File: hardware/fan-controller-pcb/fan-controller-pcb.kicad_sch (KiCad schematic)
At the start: 42 parts, among them J1 Screw_Terminal_01x04, J2 nc3fdm3-v, J3 nc3mdm3-v, SW2 SW_DIP_x10, U2 MC7805CDTG, U3 MCP4922, U4 TLC272, U5 MAX485E

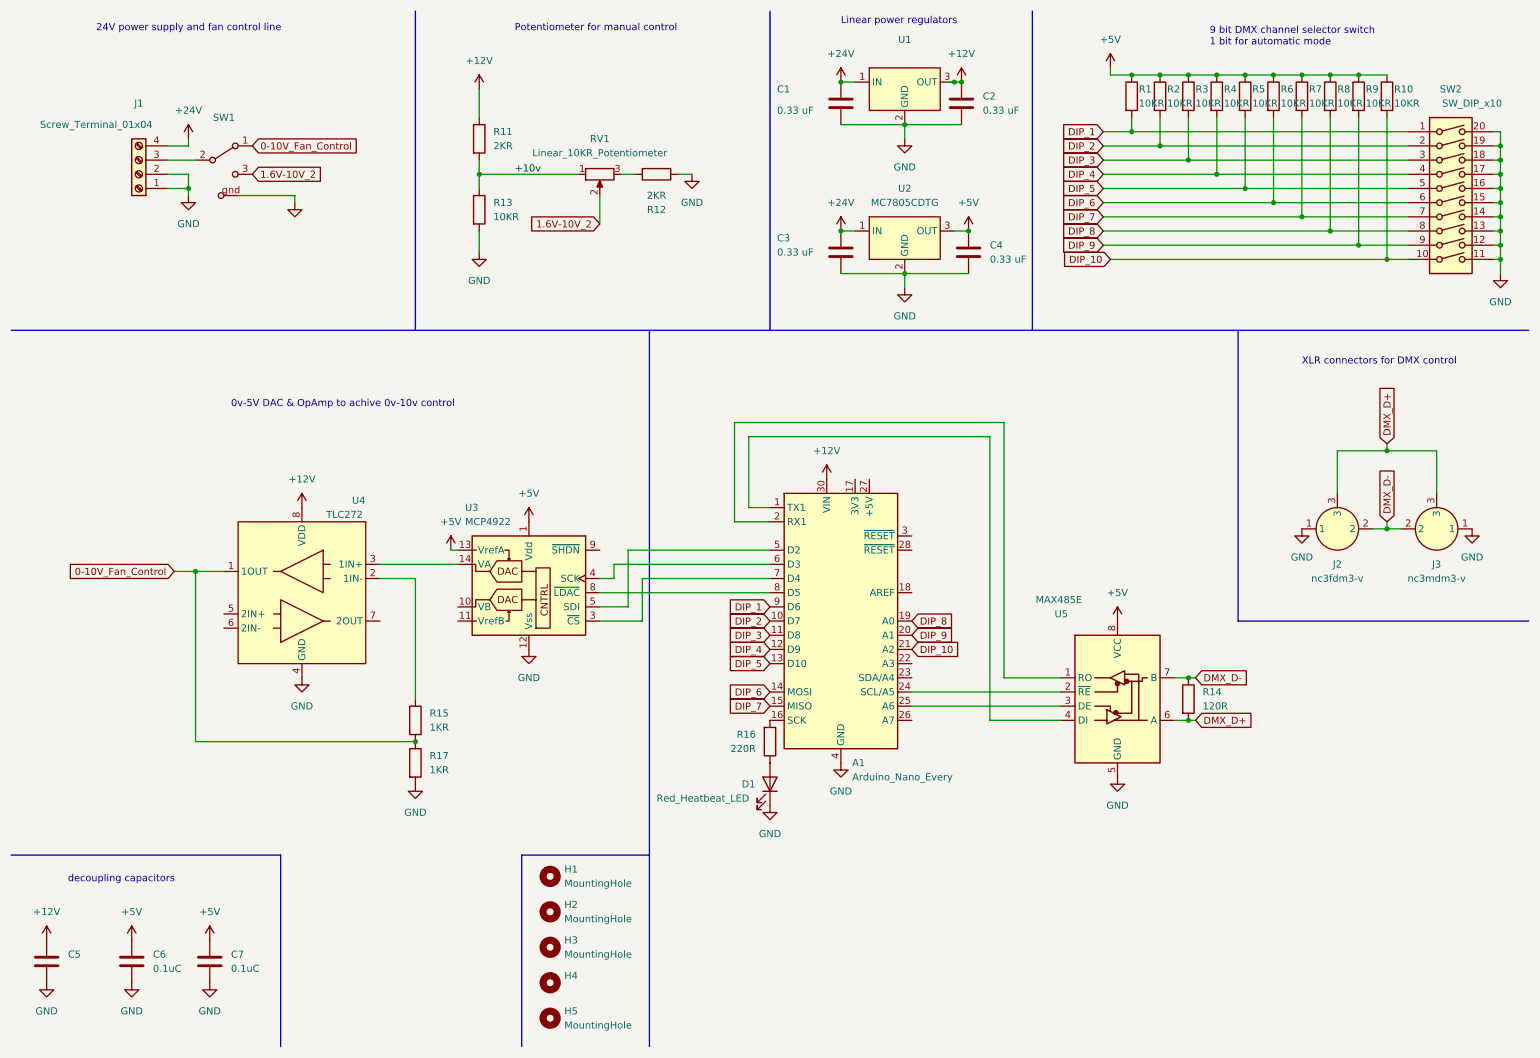
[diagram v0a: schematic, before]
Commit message: update PCB: edge cuts, routing, symbol_lib, footprint_lib, art & data sheets
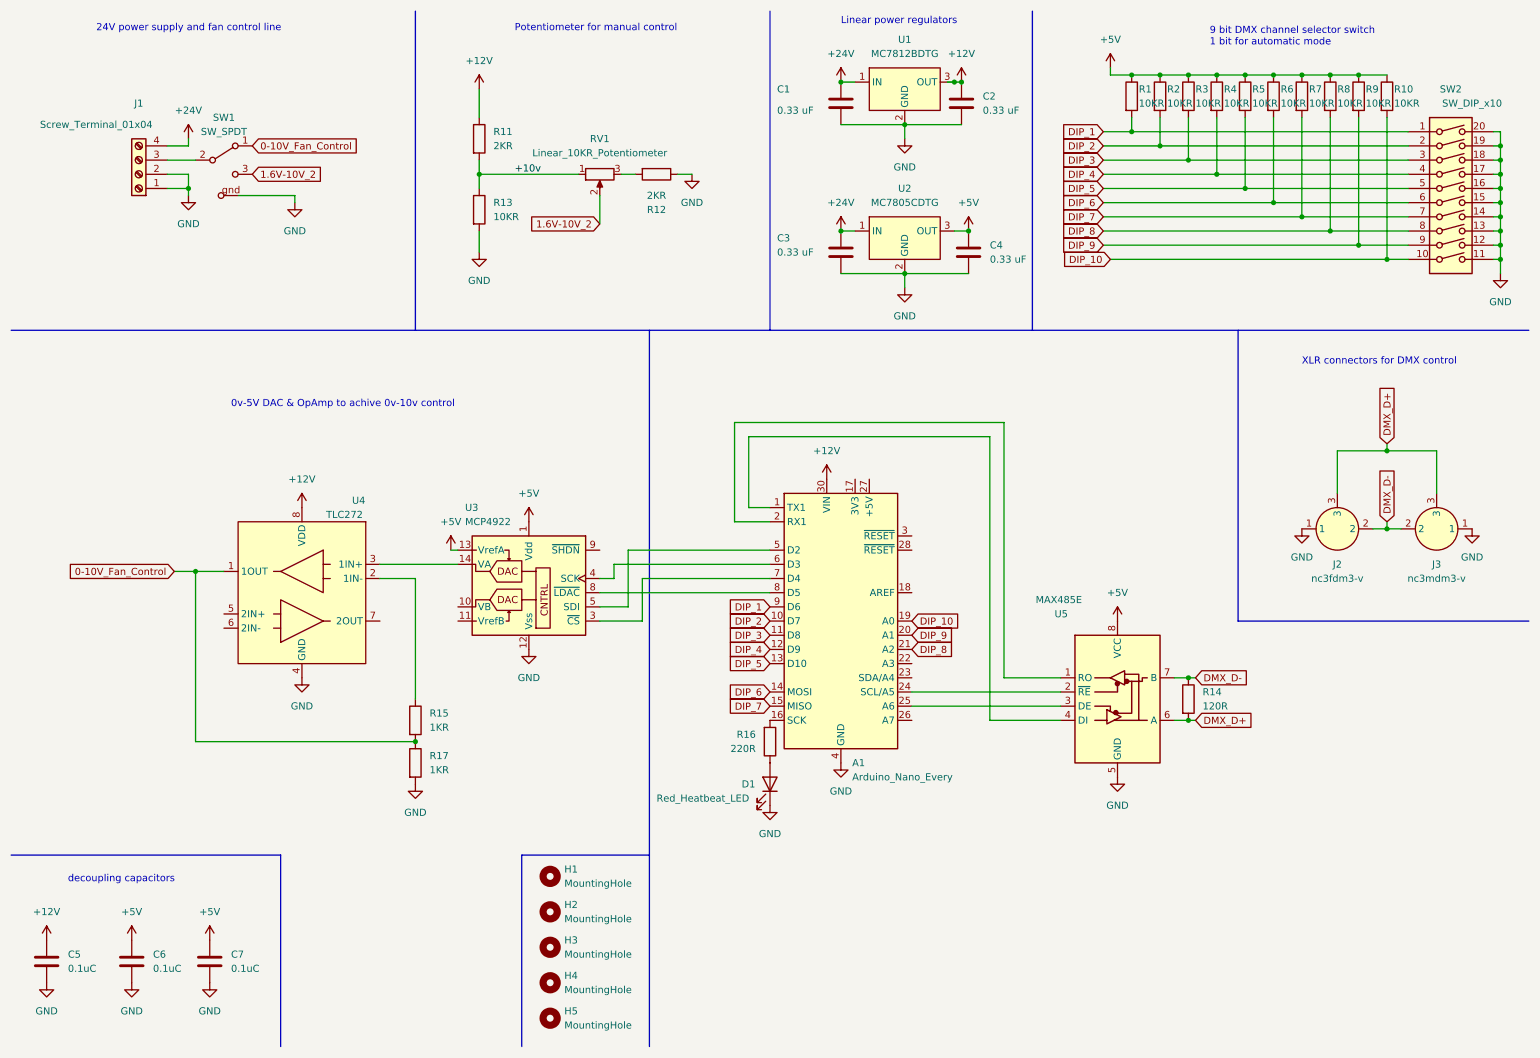
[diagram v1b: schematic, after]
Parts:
- A1: footprint (none) -> Module:Arduino_Nano
- C5: value (none) -> 0.1uC; footprint (none) -> Capacitor_SMD:C_0805_2012Metric
- C6, C7: footprint (none) -> Capacitor_SMD:C_0805_2012Metric
- H1, H2, H3, H5: footprint (none) -> MountingHole:MountingHole_3.2mm_M3_ISO14580_Pad_TopBottom
- H4: value (none) -> MountingHole; footprint (none) -> MountingHole:MountingHole_3.2mm_M3_ISO14580_Pad_TopBottom
- SW1: value (none) -> SW_SPDT; footprint (none) -> Switch:WS-TOTV_6.35_Right_Angle_Toggle_Switch
- U1: value (none) -> MC7812BDTG; footprint (none) -> Voltage_Regulator:MC7812BDTG
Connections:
- net DIP_10: now also A1.19 (A0); no longer A1.21 (A2)
- net DIP_8: now also A1.21 (A2); no longer A1.19 (A0)
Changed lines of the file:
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@@
     )
   )
-  (global_label "DIP_8" (shape input) (at 173.99 121.92 0) (fields_autoplaced)
+  (global_label "DIP_8" (shape input) (at 173.99 127 0) (fields_autoplaced)
     (effects (font (size 1.27 1.27)) (justify left))
-    (property "Intersheet References" "${INTERSHEET_REFS}" (id 0) (at 181.725 121.8406 0)
+    (property "Intersheet References" "${INTERSHEET_REFS}" (id 0) (at 181.725 126.9206 0)
       (effects (font (size 1.27 1.27)) (justify left) hide)
     )
@@
     )
   )
-  (global_label "DIP_10" (shape input) (at 173.99 127 0) (fields_autoplaced)
+  (global_label "DIP_10" (shape input) (at 173.99 121.92 0) (fields_autoplaced)
     (effects (font (size 1.27 1.27)) (justify left))
-    (property "Intersheet References" "${INTERSHEET_REFS}" (id 0) (at 182.9345 126.9206 0)
+    (property "Intersheet References" "${INTERSHEET_REFS}" (id 0) (at 182.9345 121.8406 0)
       (effects (font (size 1.27 1.27)) (justify left) hide)
     )
@@
     (in_bom yes) (on_board yes) (fields_autoplaced)
     (property "Reference" "SW1" (id 0) (at 50.8 31.75 0))
-    (property "Value" "" (id 1) (at 50.8 34.29 0))
-    (property "Footprint" "" (id 2) (at 50.8 39.37 0)
+    (property "Value" "SW_SPDT" (id 1) (at 50.8 34.29 0))
+    (property "Footprint" "Switch:WS-TOTV_6.35_Right_Angle_Toggle_Switch" (id 2) (at 50.8 39.37 0)
       (effects (font (size 1.27 1.27)) hide)
     )
@@
       (effects (font (size 1.27 1.27)) (justify left))
     )
-    (property "Footprint" "" (id 2) (at 49.2252 186.69 0)
+    (property "Footprint" "Capacitor_SMD:C_0805_2012Metric" (id 2) (at 49.2252 186.69 0)
       (effects (font (size 1.27 1.27)) hide)
     )
@@
       (effects (font (size 1.27 1.27)) (justify left))
     )
-    (property "Value" "" (id 1) (at 111.76 187.9599 0)
-      (effects (font (size 1.27 1.27)) (justify left))
-    )
-    (property "Footprint" "" (id 2) (at 109.22 186.69 0)
+    (property "Value" "MountingHole" (id 1) (at 111.76 187.9599 0)
+      (effects (font (size 1.27 1.27)) (justify left))
+    )
+    (property "Footprint" "MountingHole:MountingHole_3.2mm_M3_ISO14580_Pad_TopBottom" (id 2) (at 109.22 186.69 0)
       (effects (font (size 1.27 1.27)) hide)
     )
@@
       (effects (font (size 1.27 1.27)) (justify left))
     )
-    (property "Footprint" "" (id 2) (at 109.22 180.34 0)
+    (property "Footprint" "MountingHole:MountingHole_3.2mm_M3_ISO14580_Pad_TopBottom" (id 2) (at 109.22 180.34 0)
       (effects (font (size 1.27 1.27)) hide)
     )
@@
       (effects (font (size 1.27 1.27)) (justify left))
     )
-    (property "Footprint" "" (id 2) (at 35.2552 186.69 0)
+    (property "Footprint" "Capacitor_SMD:C_0805_2012Metric" (id 2) (at 35.2552 186.69 0)
       (effects (font (size 1.27 1.27)) hide)
     )
@@
     (in_bom yes) (on_board yes) (fields_autoplaced)
     (property "Reference" "U1" (id 0) (at 172.72 17.78 0))
-    (property "Value" "" (id 1) (at 172.72 20.32 0))
-    (property "Footprint" "" (id 2) (at 171.45 25.4 0)
+    (property "Value" "MC7812BDTG" (id 1) (at 172.72 20.32 0))
+    (property "Footprint" "Voltage_Regulator:MC7812BDTG" (id 2) (at 171.45 25.4 0)
       (effects (font (size 1.27 1.27)) hide)
     )
@@
       (effects (font (size 1.27 1.27)) (justify left))
     )
-    (property "Footprint" "" (id 2) (at 161.29 121.92 0)
+    (property "Footprint" "Module:Arduino_Nano" (id 2) (at 161.29 121.92 0)
       (effects (font (size 1.27 1.27) italic) hide)
     )
@@
       (effects (font (size 1.27 1.27)) (justify left))
     )
-    (property "Footprint" "" (id 2) (at 109.22 173.99 0)
+    (property "Footprint" "MountingHole:MountingHole_3.2mm_M3_ISO14580_Pad_TopBottom" (id 2) (at 109.22 173.99 0)
       (effects (font (size 1.27 1.27)) hide)
     )
@@
       (effects (font (size 1.27 1.27)) (justify left))
     )
-    (property "Value" "" (id 1) (at 22.86 184.1499 0)
-      (effects (font (size 1.27 1.27)) (justify left))
-    )
-    (property "Footprint" "" (id 2) (at 20.0152 186.69 0)
+    (property "Value" "0.1uC" (id 1) (at 22.86 184.1499 0)
+      (effects (font (size 1.27 1.27)) (justify left))
+    )
+    (property "Footprint" "Capacitor_SMD:C_0805_2012Metric" (id 2) (at 20.0152 186.69 0)
       (effects (font (size 1.27 1.27)) hide)
     )
@@
       (effects (font (size 1.27 1.27)) (justify left))
     )
-    (property "Footprint" "" (id 2) (at 109.22 193.04 0)
+    (property "Footprint" "MountingHole:MountingHole_3.2mm_M3_ISO14580_Pad_TopBottom" (id 2) (at 109.22 193.04 0)
       (effects (font (size 1.27 1.27)) hide)
     )
@@
       (effects (font (size 1.27 1.27)) hide)
     )
-    (property "Value" "" (id 1) (at 63.5 52.07 0))
+    (property "Value" "GND" (id 1) (at 63.5 52.07 0))
     (property "Footprint" "" (id 2) (at 63.5 46.99 0)
       (effects (font (size 1.27 1.27)) hide)
@@
       (effects (font (size 1.27 1.27)) (justify left))
     )
-    (property "Footprint" "" (id 2) (at 109.22 167.64 0)
-      (effects (font (size 1.27 1.27)) hide)
-    )
+    (property "Footprint" "MountingHole:MountingHole_3.2mm_M3_ISO14580_Pad_TopBottom" (id 2) (at 109.22 167.64 0)
+      (effects (font (size 1.27 1.27)) hide)
+    )

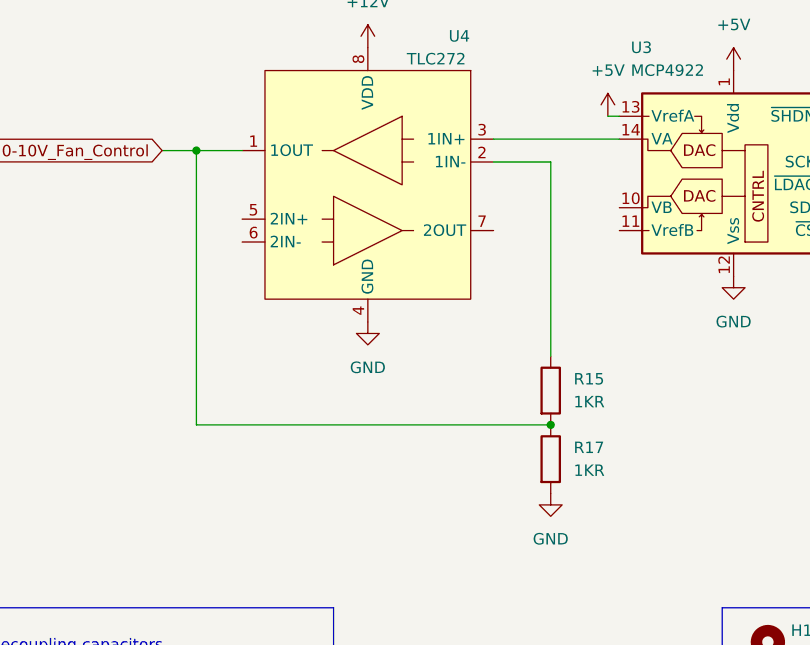
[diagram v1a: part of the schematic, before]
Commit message: Fix the OP-Amp circuit
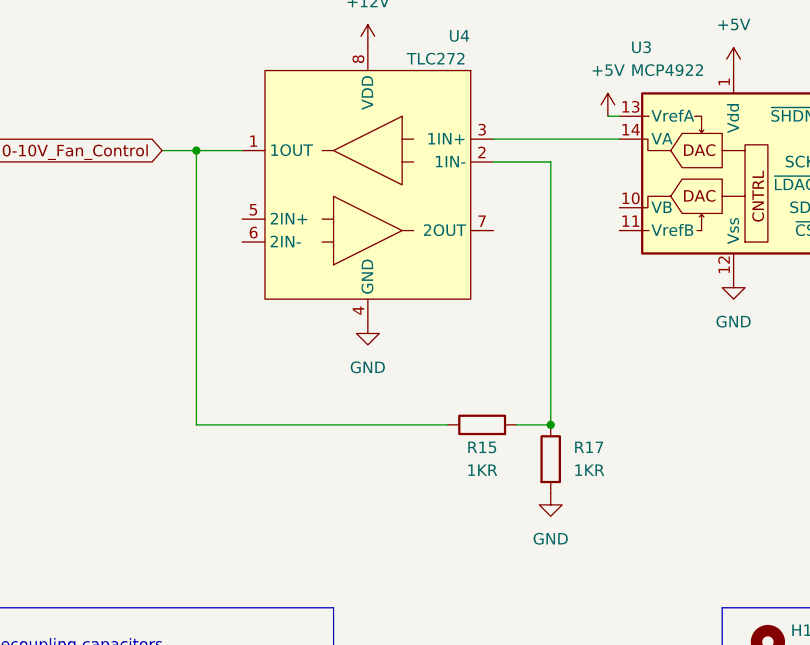
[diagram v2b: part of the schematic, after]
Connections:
- net 0-10V_Fan_Control: now also R15.1; no longer R15.2, R17.1
- net at U4.2 (1IN-): now also R15.2, R17.1; no longer R15.1
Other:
- moved on the sheet: R15
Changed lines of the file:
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@@
   (junction (at 279.4 44.45) (diameter 0) (color 0 0 0 0)
   )
+  (junction (at 254 54.61) (diameter 0) (color 0 0 0 0)
+  )
+  (junction (at 213.36 24.13) (diameter 0) (color 0 0 0 0)
+  )
+  (junction (at 223.52 24.13) (diameter 0) (color 0 0 0 0)
+  )
+  (junction (at 243.84 24.13) (diameter 0) (color 0 0 0 0)
+  )
+  (junction (at 279.4 46.99) (diameter 0) (color 0 0 0 0)
+  )
+  (junction (at 259.08 105.41) (diameter 0) (color 0 0 0 0)
+  )
+  (junction (at 248.92 52.07) (diameter 0) (color 0 0 0 0)
+  )
+  (junction (at 96.52 41.91) (diameter 0) (color 0 0 0 0)
+  )
+  (junction (at 279.4 41.91) (diameter 0) (color 0 0 0 0)
+  )
+  (junction (at 279.4 57.15) (diameter 0) (color 0 0 0 0)
+  )
+  (junction (at 223.52 139.7) (diameter 0) (color 0 0 0 0)
+  )
+  (junction (at 218.44 36.83) (diameter 0) (color 0 0 0 0)
+  )
+  (junction (at 233.68 24.13) (diameter 0) (color 0 0 0 0)
+  )
+  (junction (at 238.76 24.13) (diameter 0) (color 0 0 0 0)
+  )
   (junction (at 85.09 143.51) (diameter 0) (color 0 0 0 0)
   )
-  (junction (at 254 54.61) (diameter 0) (color 0 0 0 0)
-  )
-  (junction (at 213.36 24.13) (diameter 0) (color 0 0 0 0)
-  )
-  (junction (at 223.52 24.13) (diameter 0) (color 0 0 0 0)
-  )
-  (junction (at 243.84 24.13) (diameter 0) (color 0 0 0 0)
-  )
-  (junction (at 279.4 46.99) (diameter 0) (color 0 0 0 0)
-  )
-  (junction (at 259.08 105.41) (diameter 0) (color 0 0 0 0)
-  )
-  (junction (at 248.92 52.07) (diameter 0) (color 0 0 0 0)
-  )
-  (junction (at 96.52 41.91) (diameter 0) (color 0 0 0 0)
-  )
-  (junction (at 279.4 41.91) (diameter 0) (color 0 0 0 0)
-  )
-  (junction (at 279.4 57.15) (diameter 0) (color 0 0 0 0)
-  )
-  (junction (at 223.52 139.7) (diameter 0) (color 0 0 0 0)
-  )
-  (junction (at 218.44 36.83) (diameter 0) (color 0 0 0 0)
-  )
-  (junction (at 233.68 24.13) (diameter 0) (color 0 0 0 0)
-  )
-  (junction (at 238.76 24.13) (diameter 0) (color 0 0 0 0)
-  )
   (junction (at 228.6 41.91) (diameter 0) (color 0 0 0 0)
   )
@@
     (stroke (width 0) (type default) (color 0 0 0 0))
   )
-  (wire (pts (xy 85.09 114.3) (xy 85.09 135.89))
+  (wire (pts (xy 85.09 114.3) (xy 85.09 143.51))
     (stroke (width 0) (type default) (color 0 0 0 0))
   )
@@
     (stroke (width 0) (type default) (color 0 0 0 0))
   )
-  (wire (pts (xy 85.09 143.51) (xy 45.72 143.51))
-    (stroke (width 0) (type default) (color 0 0 0 0))
-  )
   (polyline (pts (xy 232.41 69.85) (xy 232.41 121.92))
     (stroke (width 0) (type default) (color 0 0 0 0))
   )
+  (wire (pts (xy 81.28 143.51) (xy 85.09 143.51))
+    (stroke (width 0) (type default) (color 0 0 0 0))
+  )
   (wire (pts (xy 120.65 111.76) (xy 148.59 111.76))
     (stroke (width 0) (type default) (color 0 0 0 0))
@@
   )
   (wire (pts (xy 44.45 36.83) (xy 44.45 35.56))
+    (stroke (width 0) (type default) (color 0 0 0 0))
+  )
+  (wire (pts (xy 45.72 143.51) (xy 73.66 143.51))
     (stroke (width 0) (type default) (color 0 0 0 0))
   )
@@
     (pin "1")
   )
-  (symbol (lib_id "Device:R") (at 85.09 139.7 0) (unit 1)
-    (in_bom yes) (on_board yes) (fields_autoplaced)
-    (property "Reference" "R15" (id 0) (at 87.63 138.4299 0)
-      (effects (font (size 1.27 1.27)) (justify left))
-    )
-    (property "Value" "1KR" (id 1) (at 87.63 140.9699 0)
-      (effects (font (size 1.27 1.27)) (justify left))
-    )
-    (property "Footprint" "Resistor_SMD:R_0603_1608Metric" (id 2) (at 83.312 139.7 90)
-      (effects (font (size 1.27 1.27)) hide)
-    )
-    (property "Datasheet" "~" (id 3) (at 85.09 139.7 0)
-      (effects (font (size 1.27 1.27)) hide)
-    )
+  (symbol (lib_id "Device:R") (at 77.47 143.51 90) (unit 1)
+    (in_bom yes) (on_board yes)
+    (property "Reference" "R15" (id 0) (at 77.47 146.05 90))
+    (property "Value" "1KR" (id 1) (at 77.47 148.59 90))
+    (property "Footprint" "Resistor_SMD:R_0603_1608Metric" (id 2) (at 77.47 145.288 90)
+      (effects (font (size 1.27 1.27)) hide)
+    )
+    (property "Datasheet" "~" (id 3) (at 77.47 143.51 0)
+      (effects (font (size 1.27 1.27)) hide)
+    )
